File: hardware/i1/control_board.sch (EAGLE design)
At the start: 45 parts, among them IC1 4021N, J1 AUDIO_JACK_3.5MM_KIT, P2 PTV112-4420A-A503

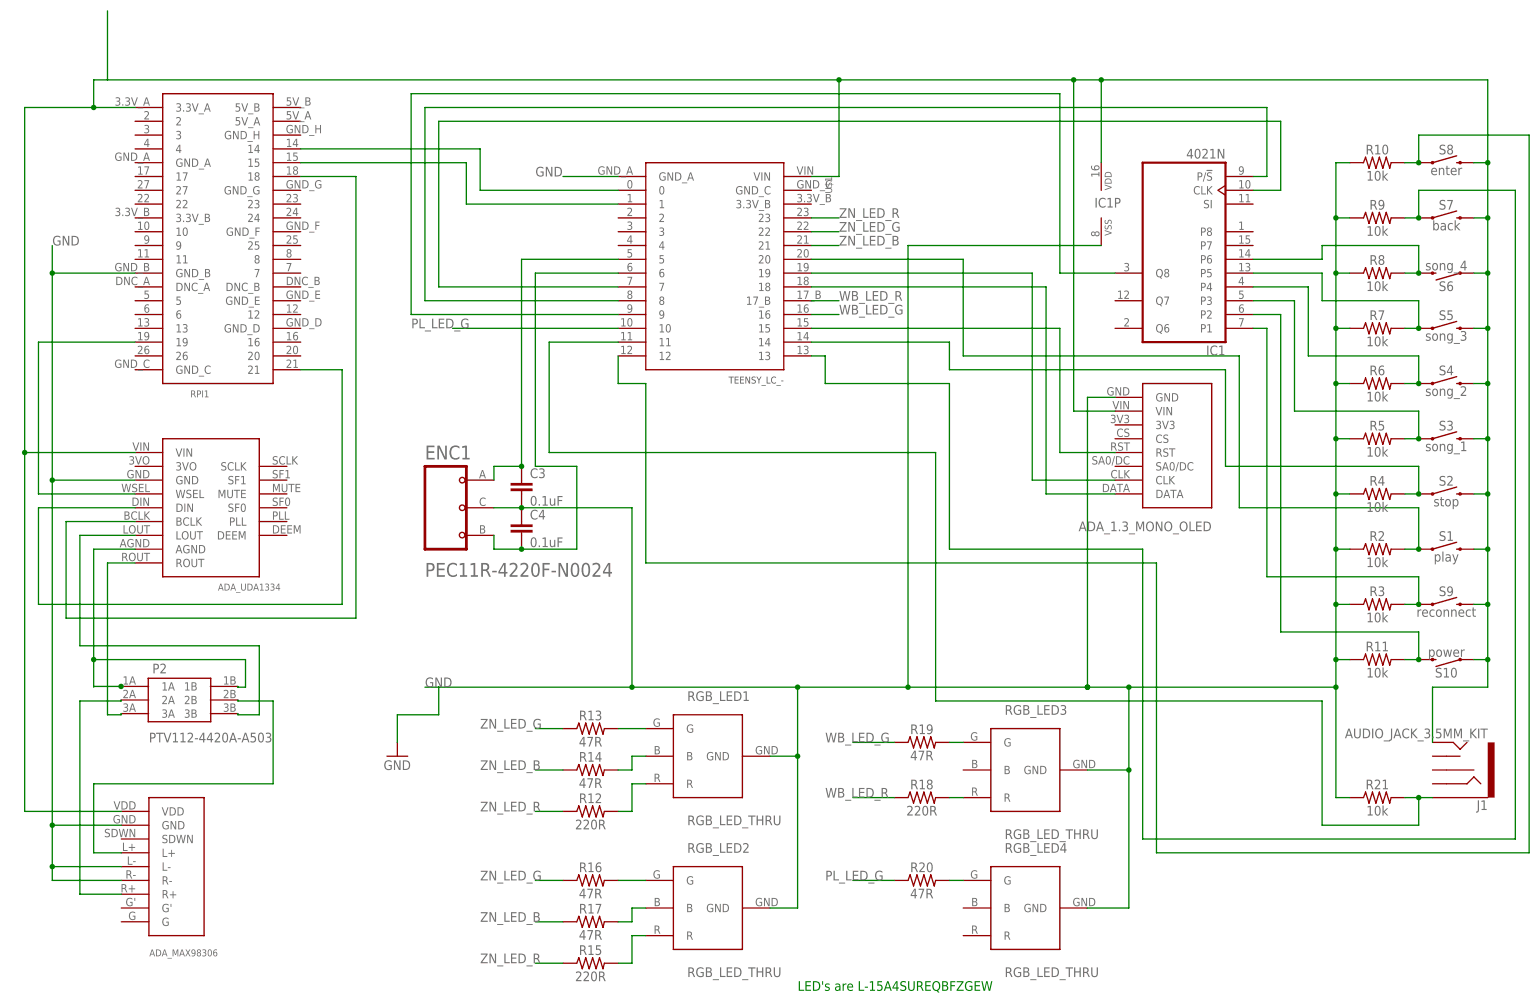
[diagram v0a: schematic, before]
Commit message: Split into two boards
Separate RPi audio hat
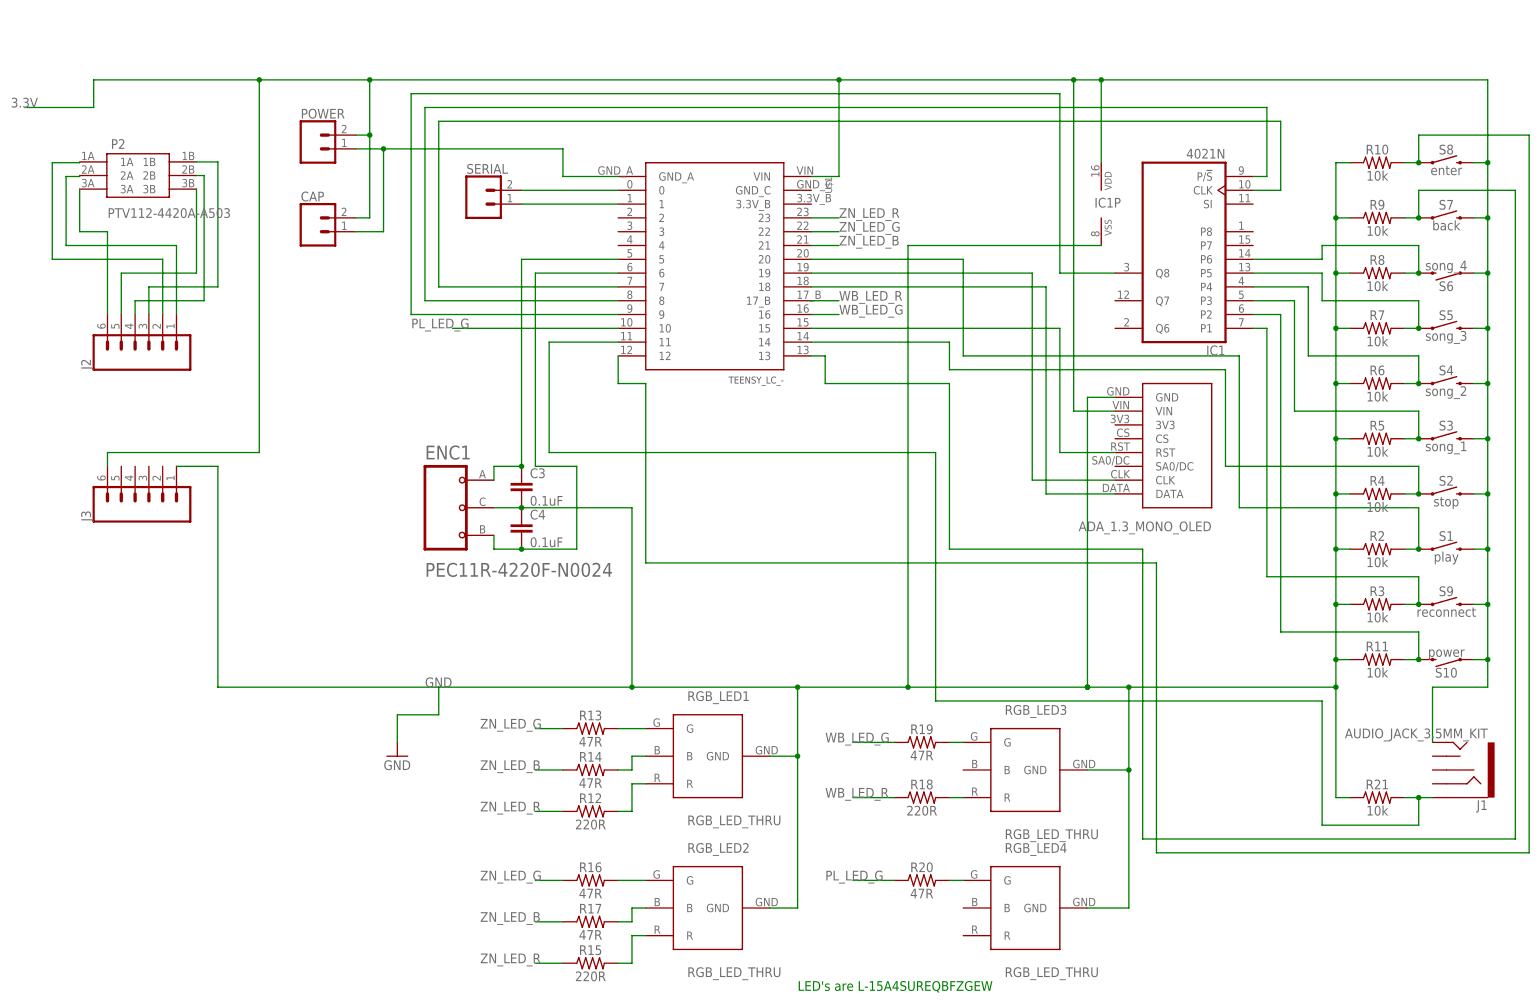
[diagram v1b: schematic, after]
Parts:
- removed MAX1: ADA_MAX98306, my_library:ADA_MAX98306
- removed RPI1: RPI_HEADER, my_library:RPI_HEADER
- removed UDA1: ADA_UDA1334, my_library:ADA_UDA1334
- added CAP, POWER, SERIAL: (no value), SparkFun-Connectors:CONN_02
- added J2, J3: (no value), SparkFun-Connectors:CONN_06NO_SILK_NO_POP
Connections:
- removed net N$36: P2.3A, UDA1.ROUT
- removed net N$37: P2.1A, P2.1B, UDA1.AGND
- removed net N$39: MAX1.L+, P2.2B
- removed net N$40: P2.3B, UDA1.LOUT
- new net 3.3V: CAP.2, IC1P.VDD, J1.TIP, J3.6, OLED1.VIN, POWER.2, S1.2, S10.1, S2.2, S3.2, S4.2, S5.2, S6.1, S7.2, S8.2, S9.2, U$1.VIN
- new net N$32: J2.1, P2.2A
- net GND: now also CAP.1, J3.1, POWER.1; no longer MAX1.GND, MAX1.L-, MAX1.R-, RPI1.GND_B, UDA1.GND
- net N$17: now also SERIAL.1, U$1.1; no longer IC1P.VDD, J1.TIP, MAX1.VDD, OLED1.VIN, RPI1.3.3V_A, S1.2, S10.1, S2.2, S3.2, S4.2, S5.2, S6.1, S7.2, S8.2, S9.2, U$1.VIN, UDA1.VIN
- net N$28: now also SERIAL.2; no longer RPI1.14
- net N$29: now also J2.2, P2.1A; no longer RPI1.15, U$1.1
- net N$33: now also J2.6, P2.3A; no longer RPI1.19, UDA1.WSEL
- net N$34: now also J2.4, P2.2B; no longer RPI1.21, UDA1.DIN
- net N$35: now also J2.5, P2.3B; no longer RPI1.18, UDA1.BCLK
- net N$38: now also J2.3, P2.1B; no longer MAX1.R+, P2.2A
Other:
- moved on the sheet: P2

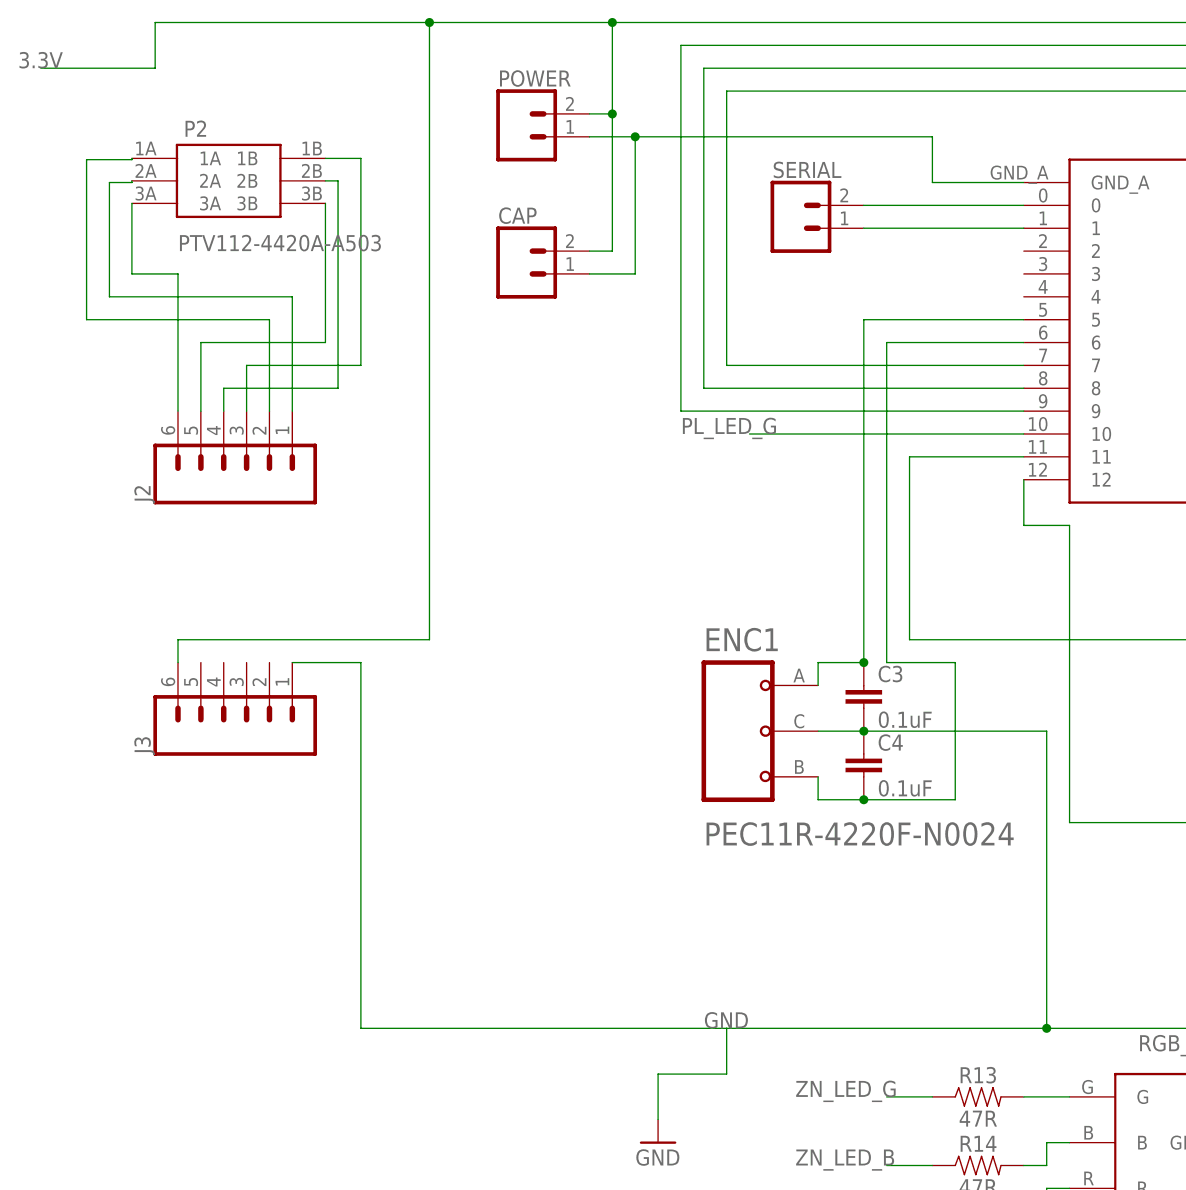
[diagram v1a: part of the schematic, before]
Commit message: Add wristband schematic and board layout
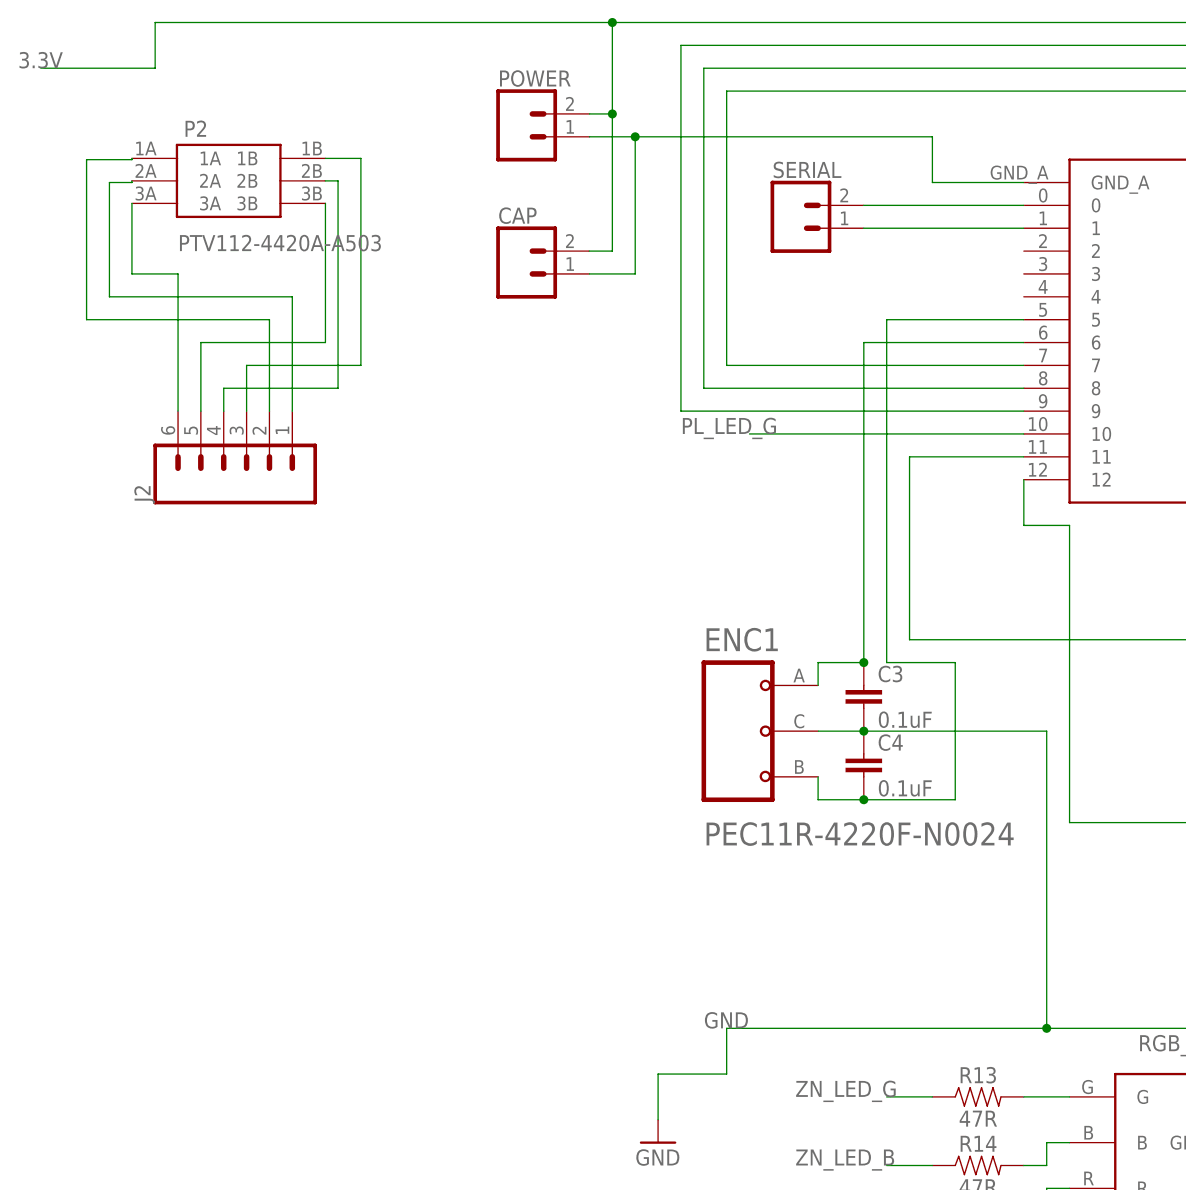
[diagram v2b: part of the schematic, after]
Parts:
- removed J3: (no value), SparkFun-Connectors:CONN_06NO_SILK_NO_POP
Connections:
- net 3.3V: no longer J3.6
- net GND: no longer J3.1
- net N$19: now also U$1.6; no longer U$1.5
- net N$20: now also U$1.5; no longer U$1.6
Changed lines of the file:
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@@
 <part name="CAP" library="SparkFun-Connectors" library_urn="urn:adsk.eagle:library:513" deviceset="CONN_02" device="" package3d_urn="urn:adsk.eagle:package:38039/1"/>
 <part name="J2" library="SparkFun-Connectors" library_urn="urn:adsk.eagle:library:513" deviceset="CONN_06" device="NO_SILK_NO_POP" package3d_urn="urn:adsk.eagle:package:38130/1"/>
-<part name="J3" library="SparkFun-Connectors" library_urn="urn:adsk.eagle:library:513" deviceset="CONN_06" device="NO_SILK_NO_POP" package3d_urn="urn:adsk.eagle:package:38130/1"/>
 </parts>
 <sheets>
@@
 <attribute name="VALUE" x="-2.794" y="116.84" size="1.778" layer="96" font="vector" rot="R90"/>
 <attribute name="NAME" x="-23.368" y="116.84" size="1.778" layer="95" font="vector" rot="R90"/>
-</instance>
-<instance part="J3" gate="G$1" x="-12.7" y="93.98" smashed="yes" rot="R90">
-<attribute name="VALUE" x="-2.794" y="88.9" size="1.778" layer="96" font="vector" rot="R90"/>
-<attribute name="NAME" x="-23.368" y="88.9" size="1.778" layer="95" font="vector" rot="R90"/>
 </instance>
 </instances>
@@
 </segment>
 </net>
-<net name="N$19" class="0">
-<segment>
-<pinref part="C3" gate="G$1" pin="1"/>
-<wire x1="55.88" y1="99.06" x2="55.88" y2="137.16" width="0.1524" layer="91"/>
-<pinref part="ENC1" gate="G$1" pin="CHANNEL_A"/>
-<wire x1="50.8" y1="96.52" x2="50.8" y2="99.06" width="0.1524" layer="91"/>
-<wire x1="50.8" y1="99.06" x2="55.88" y2="99.06" width="0.1524" layer="91"/>
-<junction x="55.88" y="99.06"/>
-<wire x1="73.66" y1="137.16" x2="55.88" y2="137.16" width="0.1524" layer="91"/>
-<pinref part="U$1" gate="G$1" pin="5"/>
-</segment>
-</net>
 <net name="N$20" class="0">
 <segment>
@@
 <wire x1="66.04" y1="83.82" x2="66.04" y2="99.06" width="0.1524" layer="91"/>
 <wire x1="66.04" y1="99.06" x2="58.42" y2="99.06" width="0.1524" layer="91"/>
-<wire x1="58.42" y1="99.06" x2="58.42" y2="134.62" width="0.1524" layer="91"/>
-<wire x1="73.66" y1="134.62" x2="58.42" y2="134.62" width="0.1524" layer="91"/>
-<pinref part="U$1" gate="G$1" pin="6"/>
+<wire x1="58.42" y1="99.06" x2="58.42" y2="137.16" width="0.1524" layer="91"/>
+<wire x1="73.66" y1="137.16" x2="58.42" y2="137.16" width="0.1524" layer="91"/>
+<pinref part="U$1" gate="G$1" pin="5"/>
 </segment>
 </net>
@@
 <wire x1="127" y1="139.7" x2="127" y2="58.42" width="0.1524" layer="91"/>
 <junction x="127" y="58.42"/>
-<wire x1="40.64" y1="58.42" x2="0" y2="58.42" width="0.1524" layer="91"/>
-<wire x1="0" y1="58.42" x2="0" y2="99.06" width="0.1524" layer="91"/>
-<pinref part="J3" gate="G$1" pin="1"/>
-<wire x1="0" y1="99.06" x2="-7.62" y2="99.06" width="0.1524" layer="91"/>
 </segment>
 </net>
@@
 <pinref part="S6" gate="G$1" pin="1"/>
 <wire x1="114.3" y1="170.18" x2="27.94" y2="170.18" width="0.1524" layer="91"/>
-<wire x1="27.94" y1="170.18" x2="7.62" y2="170.18" width="0.1524" layer="91"/>
-<wire x1="7.62" y1="170.18" x2="-22.86" y2="170.18" width="0.1524" layer="91"/>
+<wire x1="27.94" y1="170.18" x2="-22.86" y2="170.18" width="0.1524" layer="91"/>
 <wire x1="231.14" y1="134.62" x2="233.68" y2="134.62" width="0.1524" layer="91"/>
 <junction x="233.68" y="134.62"/>
@@
 <pinref part="CAP" gate="G$1" pin="2"/>
 <wire x1="27.94" y1="144.78" x2="25.4" y2="144.78" width="0.1524" layer="91"/>
-<wire x1="7.62" y1="170.18" x2="7.62" y2="101.6" width="0.1524" layer="91"/>
-<wire x1="7.62" y1="101.6" x2="-20.32" y2="101.6" width="0.1524" layer="91"/>
-<junction x="7.62" y="170.18"/>
-<pinref part="J3" gate="G$1" pin="6"/>
-<wire x1="-20.32" y1="101.6" x2="-20.32" y2="99.06" width="0.1524" layer="91"/>
 </segment>
 </net>
@@
 </segment>
 </net>
+<net name="N$19" class="0">
+<segment>
+<pinref part="C3" gate="G$1" pin="1"/>
+<wire x1="55.88" y1="99.06" x2="55.88" y2="134.62" width="0.1524" layer="91"/>
+<junction x="55.88" y="99.06"/>
+<wire x1="50.8" y1="99.06" x2="55.88" y2="99.06" width="0.1524" layer="91"/>
+<pinref part="ENC1" gate="G$1" pin="CHANNEL_A"/>
+<wire x1="50.8" y1="96.52" x2="50.8" y2="99.06" width="0.1524" layer="91"/>
+<pinref part="U$1" gate="G$1" pin="6"/>
+<wire x1="73.66" y1="134.62" x2="55.88" y2="134.62" width="0.1524" layer="91"/>
+</segment>
+</net>

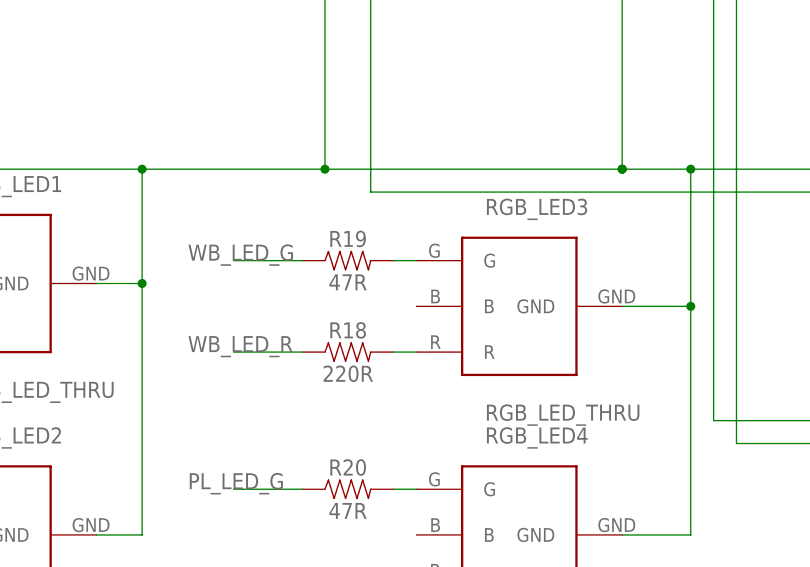
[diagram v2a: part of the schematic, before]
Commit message: Change pad size of LEDs
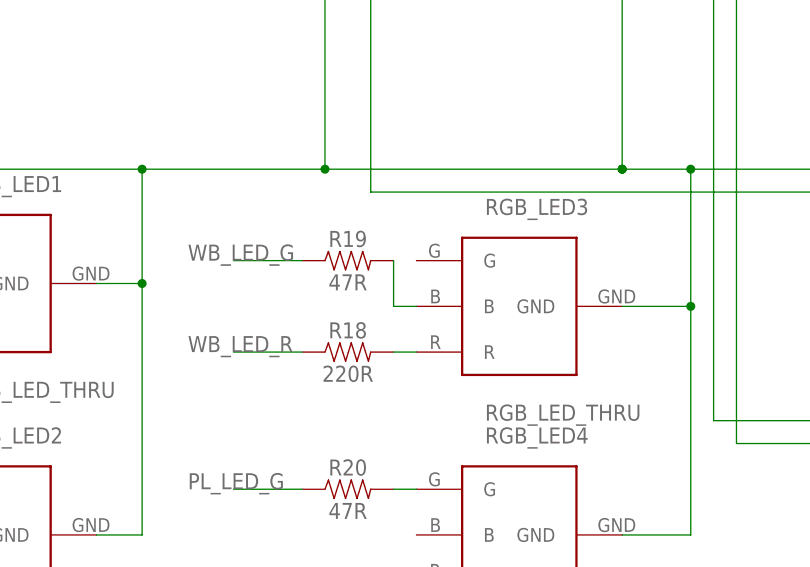
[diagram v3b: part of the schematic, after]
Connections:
- net N$24: now also RGB_LED3.B; no longer RGB_LED3.G
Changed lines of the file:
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@@
-</segment>
-</net>
-<net name="N$24" class="0">
-<segment>
-<pinref part="R19" gate="G$1" pin="2"/>
-<pinref part="RGB_LED3" gate="G$1" pin="G"/>
-<wire x1="134.62" y1="48.26" x2="137.16" y2="48.26" width="0.1524" layer="91"/>
 </segment>
 </net>
@@
 </segment>
 </net>
+<net name="N$24" class="0">
+<segment>
+<pinref part="R19" gate="G$1" pin="2"/>
+<wire x1="134.62" y1="48.26" x2="134.62" y2="43.18" width="0.1524" layer="91"/>
+<pinref part="RGB_LED3" gate="G$1" pin="B"/>
+<wire x1="134.62" y1="43.18" x2="137.16" y2="43.18" width="0.1524" layer="91"/>
+</segment>
+</net>
